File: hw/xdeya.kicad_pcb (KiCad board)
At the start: 2 copper layers, 86.2 x 48.5 mm, 71 parts, among them J2 display, J3 antenna, J4 USB_B_Micro, J5 battery, J6 A, J7 K, Q5 UMH3N, SW3 btn-up, SW4 btn-sel, SW5 btn-down, U1 ESP32-WROOM-32, U10 AXP2101, U2 LSM303AGR, U4 BMP280, U5 PCF8563T, U6 NEO-M8N, U7 CP2102, Y1 32768

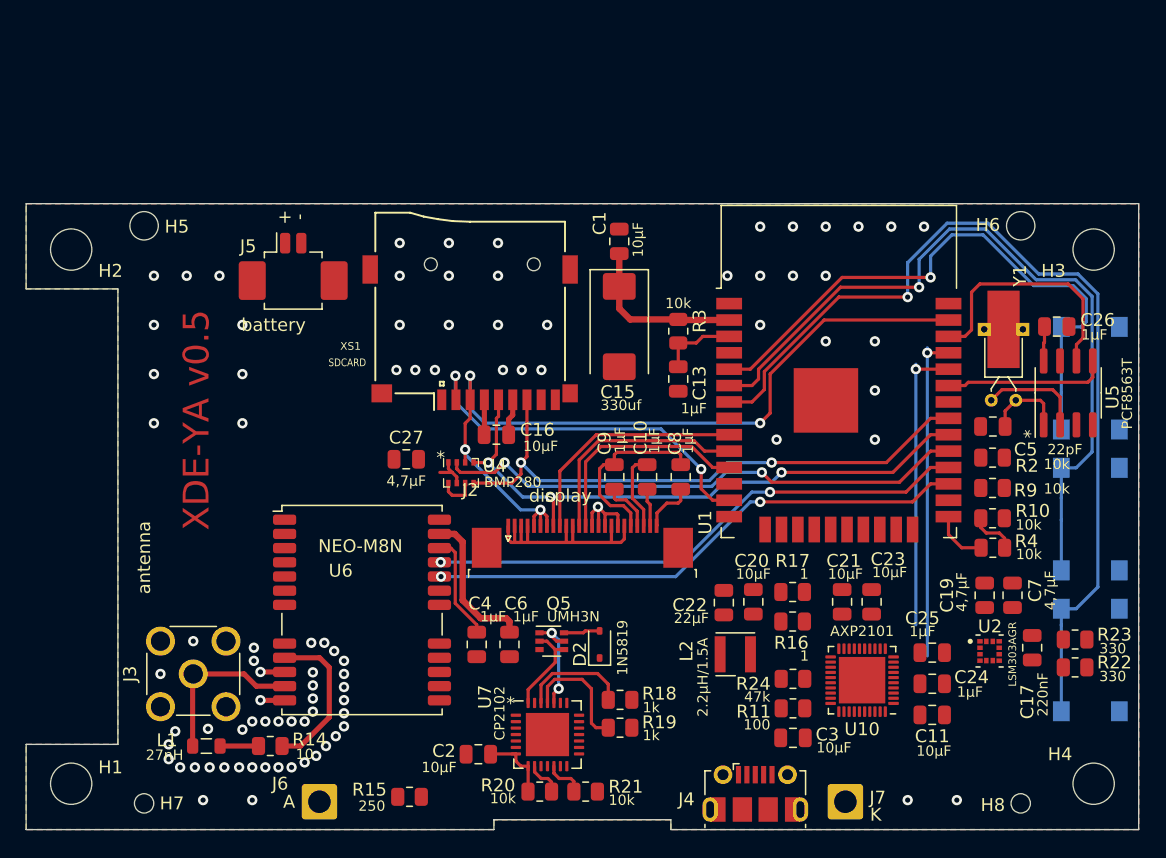
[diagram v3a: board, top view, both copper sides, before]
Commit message: hw - доделана трассировка платы, но скорее всего, придётся всё переделывать, слишком много пересечений
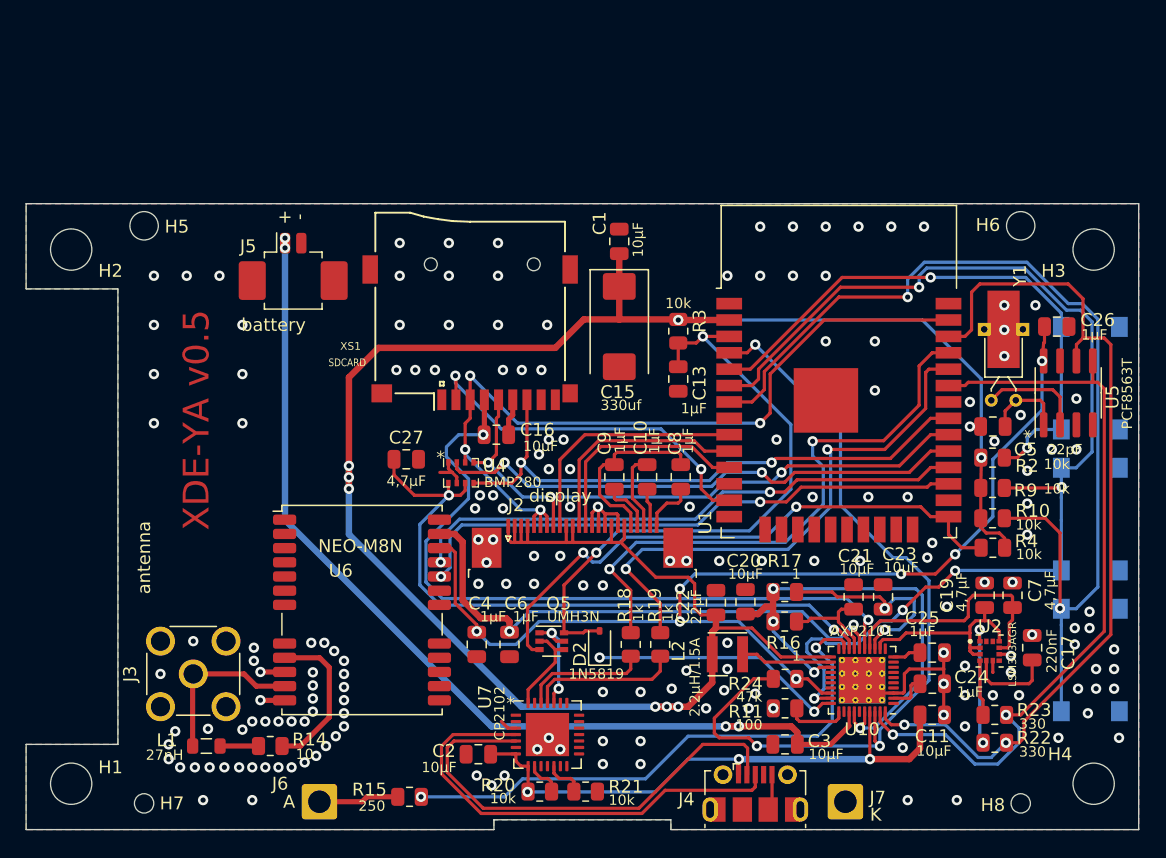
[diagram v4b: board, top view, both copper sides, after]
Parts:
- U10: footprint Package_DFN_QFN:QFN-40-1EP_5x5mm_P0.4mm_EP3.6x3.6mm -> Package_DFN_QFN:QFN-40-1EP_5x5mm_P0.4mm_EP3.6x3.6mm_ThermalVias
- moved R22 8.54 mm to (124.9, 79.4)
- moved R23 8.54 mm to (124.9, 77.2)
- moved R19 7.17 mm to (98.9, 71.8), turned to 90 degrees
- moved R18 4.37 mm to (96.6, 71.8), turned to 90 degrees
- moved C21 0.97 mm to (113.9, 68.1)
- moved C23 0.97 mm to (116.2, 68.1)
- moved C3 0.79 mm to (108.6, 79.5)
- moved R16 0.61 mm to (108.6, 70.0)
- moved R17 0.61 mm to (108.6, 67.7)
- moved C20 0.61 mm to (105.5, 68.5)
- moved C22 0.61 mm to (103.3, 68.5)
- moved L2 0.61 mm to (104.1, 72.5)
- moved R11 0.61 mm to (108.6, 76.7)
- moved R24 0.61 mm to (108.6, 74.4)
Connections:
- net Net-(J5-Pin_1) renamed /batt
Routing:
- net +3.3V: track 35.9 -> 171.7 mm, vias 0 -> 8
- net /batt: track 0.00 -> 76.0 mm, vias 0 -> 4
- net VRTC: track 10.9 -> 84.7 mm, vias 0 -> 7
- net CHRGIRQ: track 0.00 -> 64.4 mm, vias 0 -> 3
- net VSDCARD: track 2.72 -> 56.6 mm, vias 0 -> 2
- net VBMP: track 3.04 -> 52.7 mm, vias 0 -> 2
- net i2c-scl: track 19.3 -> 68.2 mm, vias 0 -> 2
- net i2c-sda: track 12.7 -> 59.4 mm, vias 0 -> 2
- net DLIGHT: track 0.00 -> 43.6 mm, vias 0 -> 2
- net /s-boot: track 4.34 -> 45.1 mm, vias 0 -> 2
- net VSYS: track 0.00 -> 39.7 mm, vias 0 -> 4
- net VBUS: track 5.61 -> 45.0 mm, vias 0 -> 3
- net /s-en: track 8.82 -> 47.9 mm, vias 0 -> 2
- net Net-(J4-D-): track 0.00 -> 36.1 mm
- net Net-(J4-D+): track 0.00 -> 35.7 mm
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
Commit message: hw - переделана трассировка платы, стало лучше, осталось: расставить шелкографию, проверить, наделать переходных по gnd
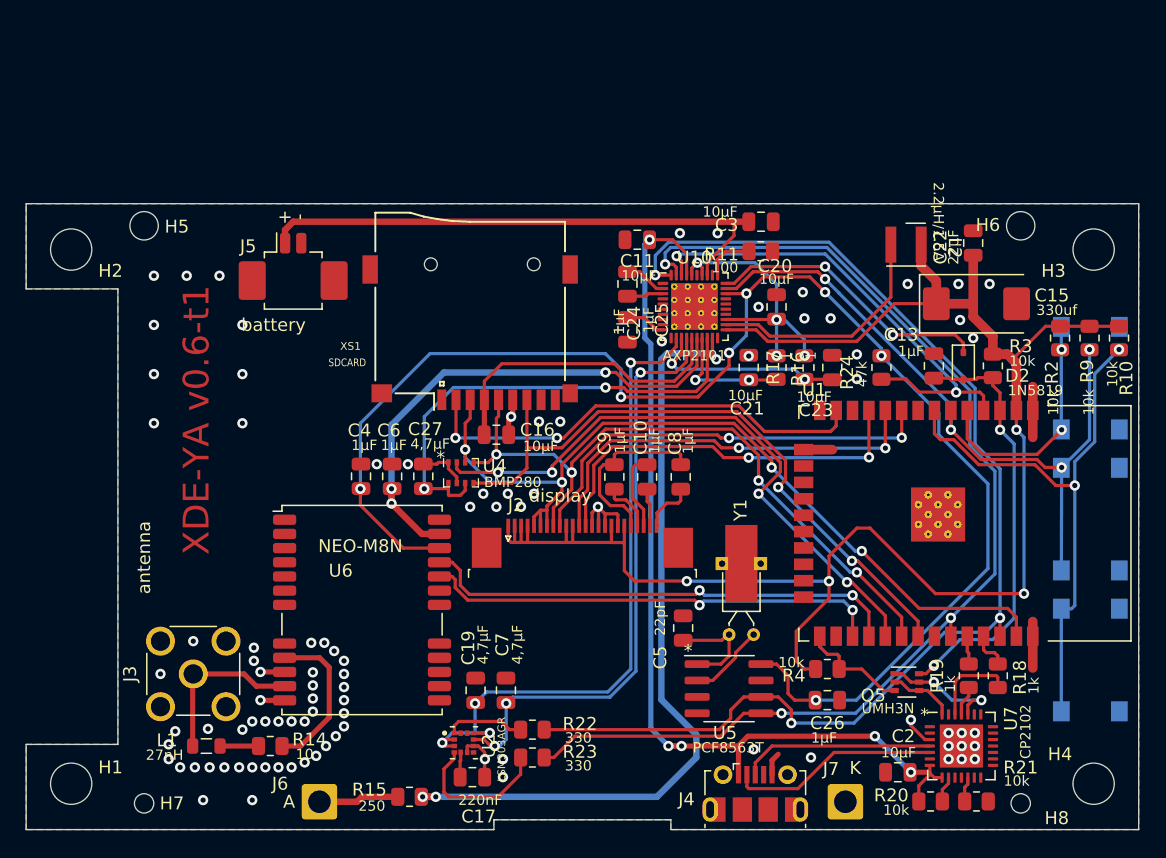
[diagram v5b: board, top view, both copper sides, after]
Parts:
- removed C1: 10μF, Capacitor_SMD:C_0805_2012Metric
- moved C17 44.5 mm to (84.4, 82.0), turned to 0 degrees
- moved C11 43.3 mm to (97.2, 40.4)
- moved U2 41.4 mm to (83.7, 79.4)
- moved C3 40.6 mm to (106.7, 39.0), turned to 0 degrees
- moved C19 40.1 mm to (84.6, 75.3)
- moved C7 39.9 mm to (87.0, 75.3)
- moved C24 39.0 mm to (96.4, 43.8), turned to -90 degrees
- moved R23 36.0 mm to (89.0, 80.5)
- moved R22 35.9 mm to (89.0, 78.4)
- moved D2 35.5 mm to (122.4, 50.2), turned to -90 degrees
- moved R11 35.5 mm to (106.7, 41.3)
- moved U5 34.9 mm to (104.3, 75.2), turned to 0 degrees
- moved L2 34.6 mm to (118.0, 40.8), turned to 0 degrees
- moved C25 34.4 mm to (96.4, 47.4), turned to -90 degrees
- moved C22 34.3 mm to (123.2, 40.6)
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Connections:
- C11 pad 1: VBUS -> GND
- C11 pad 2: GND -> VBUS
- C13 pad 1: /s-en -> GND
- C13 pad 2: GND -> /s-en
- C21 pad 1: Net-(U10-ALDOIN) -> GND
- C21 pad 2: GND -> Net-(U10-ALDOIN)
- C23 pad 1: Net-(U10-BLDOIN) -> GND
- C23 pad 2: GND -> Net-(U10-BLDOIN)
- C5 pad 1: Net-(U5-OSCI) -> GND
- C5 pad 2: GND -> Net-(U5-OSCI)
- R11 pad 1: GND -> Net-(U10-TS)
- R11 pad 2: Net-(U10-TS) -> GND
- R16 pad 1: Net-(U10-ALDOIN) -> VSYS
- R16 pad 2: VSYS -> Net-(U10-ALDOIN)
- R17 pad 1: Net-(U10-BLDOIN) -> VSYS
- R17 pad 2: VSYS -> Net-(U10-BLDOIN)
- R24 pad 1: CHRGIRQ -> VRTC
- R24 pad 2: VRTC -> CHRGIRQ
- Y1 pad 1: Net-(U5-OSCI) -> Net-(U5-OSCO)
- Y1 pad 2: Net-(U5-OSCO) -> Net-(U5-OSCI)
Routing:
- net /s-tx: track 44.7 -> 2.98 mm, vias 2 -> 0
- net +3.3V: track 171.7 -> 130.3 mm, vias 8 -> 4
- net /s-rx: track 42.2 -> 2.20 mm, vias 2 -> 0
- net /s-boot: track 45.1 -> 8.60 mm, vias 2 -> 0
- net PWROK: track 88.8 -> 53.6 mm, vias 5 -> 4
- net VCOMP-IO: track 15.9 -> 51.1 mm, vias 0 -> 4
- net /b-down: track 79.6 -> 44.9 mm
- net /batt: track 76.0 -> 42.2 mm, vias 4 -> 0
- net VSDCARD: track 56.6 -> 24.1 mm, vias 2 -> 0
- net VBUS: track 45.0 -> 74.5 mm, vias 3 -> 5
- net VRTC: track 84.7 -> 113.9 mm
- net i2c-sda: track 59.4 -> 88.1 mm, vias 2 -> 3
- net VCOMP-SUPP: track 19.1 -> 45.9 mm, vias 0 -> 3
- net CHRGIRQ: track 64.4 -> 37.8 mm, vias 3 -> 2
- net i2c-scl: track 68.2 -> 94.2 mm, vias 2 -> 3
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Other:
- board text added: "XDE-YA v0.6-t1"
- board text removed: "XDE-YA v0.5"

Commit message: hw - поправлены ошибки
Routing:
- net GND: track 37.8 -> 40.1 mm, vias 95 -> 94

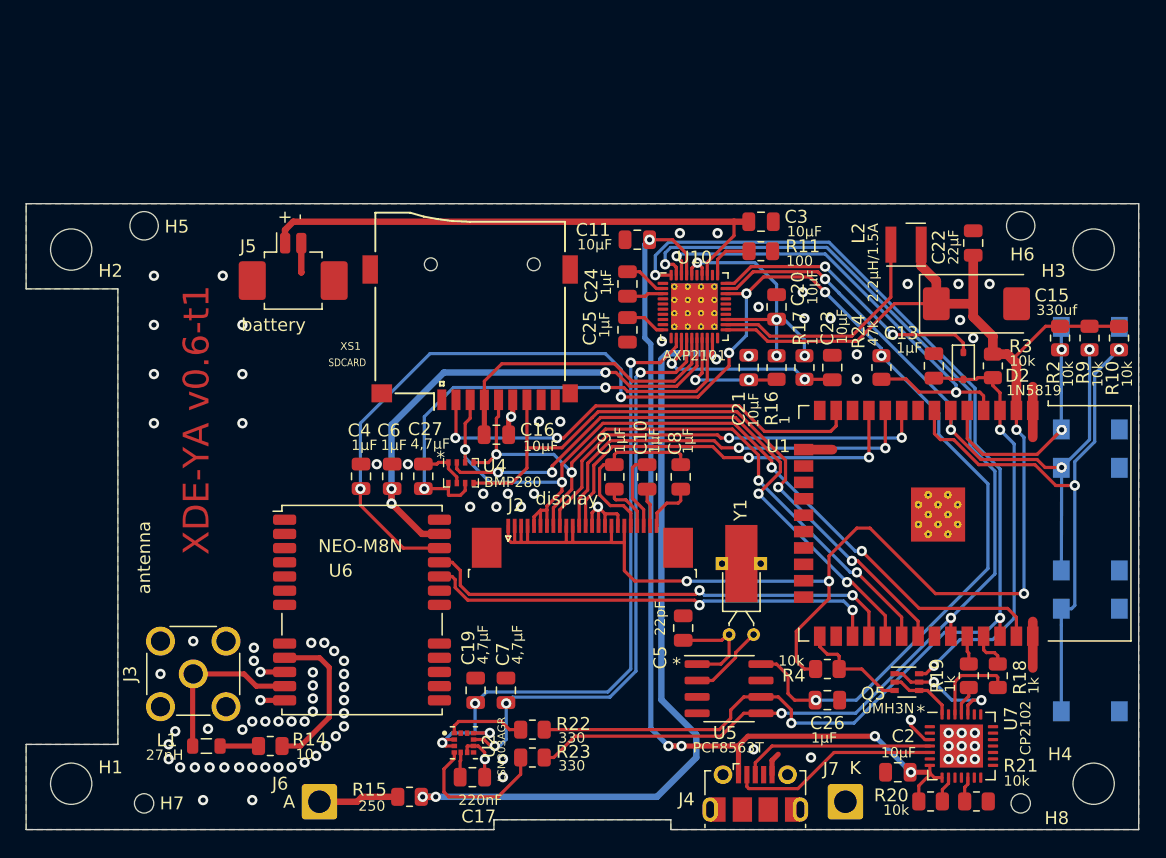
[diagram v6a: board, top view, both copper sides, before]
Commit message: hw - оптимизированы дорожки, добавлены переходные между gnd
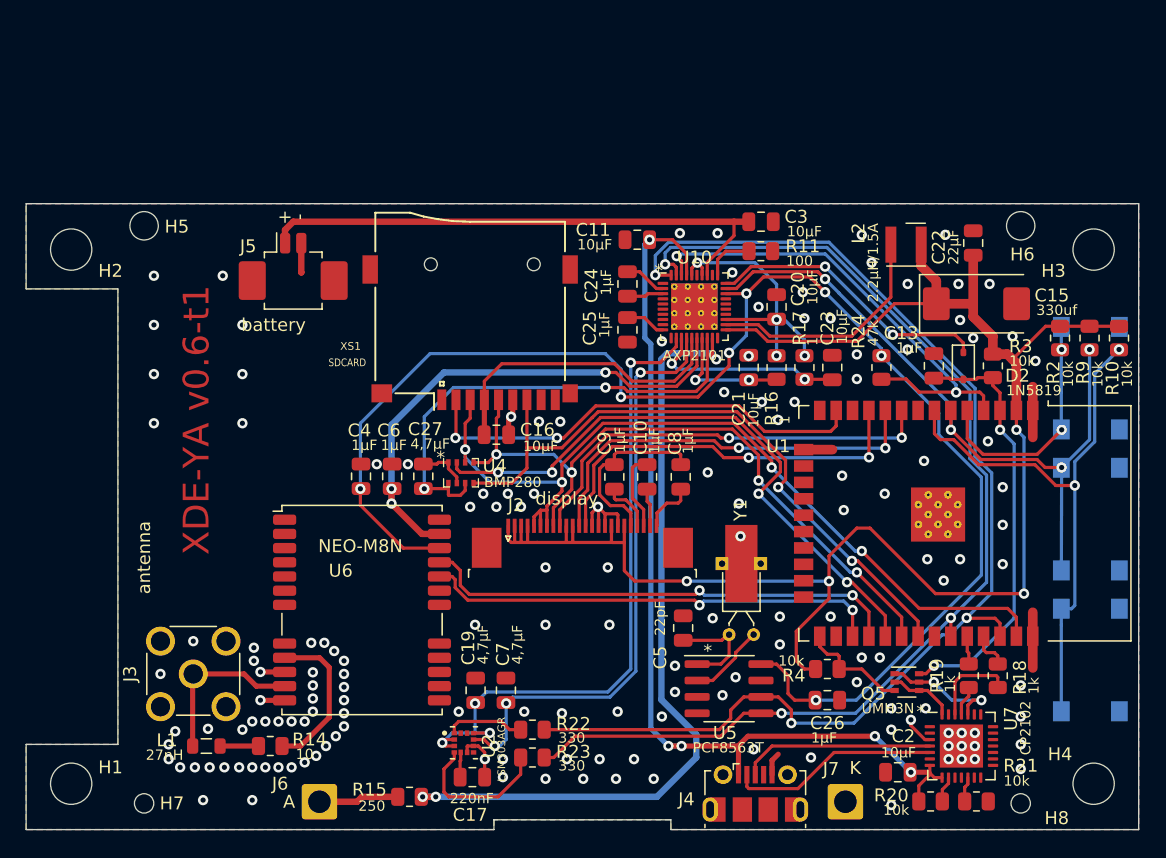
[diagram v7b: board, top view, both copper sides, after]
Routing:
- net GND: track 40.1 -> 40.8 mm, vias 94 -> 155
- net i2c-sda: track 88.1 -> 87.6 mm
